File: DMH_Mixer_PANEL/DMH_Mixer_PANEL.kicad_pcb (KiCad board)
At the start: 2 copper layers, 50 x 200 mm, 20 parts, among them J0 Panel_GND_Solder_Wire_Pad

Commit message: Finalization in progress
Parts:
- removed H10: Clip Amt, SynthStuff:MountingHole_TrimPot
- H9: footprint SynthStuff:Jack_6.35mm_Cutout_Output_v6 -> SynthStuff:Toggle_Switch_Cutout
- moved H7 37.8 mm to (58.5, 208.8)
- moved H9 24.8 mm to (91.5, 190.2)
- moved H15 16.5 mm to (75.0, 208.8)
- moved H16 0.75 mm to (83.2, 165.0)
- moved H19 0.75 mm to (58.5, 165.0)
- moved H13 0.50 mm to (83.2, 129.5)
- moved H18 0.50 mm to (58.5, 129.5)
- moved H12 0.25 mm to (83.2, 94.0)
- moved H17 0.25 mm to (58.5, 94.0)

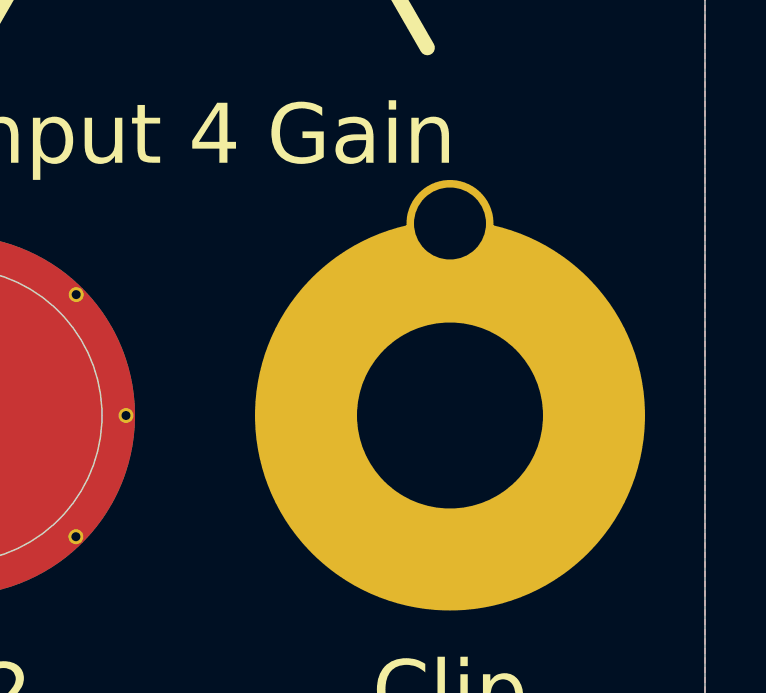
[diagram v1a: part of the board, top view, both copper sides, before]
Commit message: Panel and Connectors PCB ready
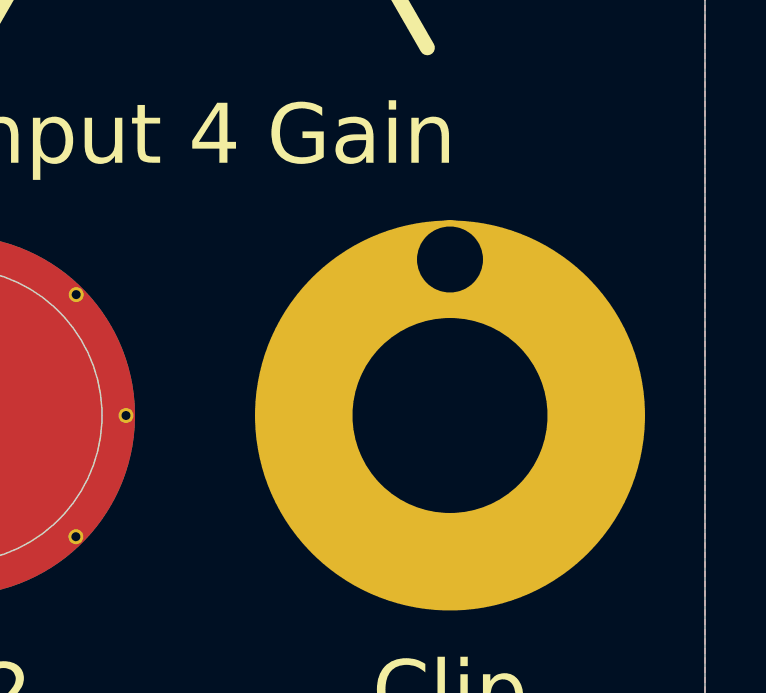
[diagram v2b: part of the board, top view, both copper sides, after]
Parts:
- H9: footprint SynthStuff:Toggle_Switch_Cutout -> SynthStuff:Toggle_Switch_APEM_Cutout
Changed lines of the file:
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@@
 		)
 	)
-	(footprint "SynthStuff:Toggle_Switch_Cutout"
+	(footprint "SynthStuff:Toggle_Switch_APEM_Cutout"
 		(layer "F.Cu")
 		(at 91.5 190.25)
@@
 			)
 		)
-		(property "Footprint" "SynthStuff:Toggle_Switch_Cutout"
+		(property "Footprint" "SynthStuff:Toggle_Switch_APEM_Cutout"
 			(at 0 0 0)
 			(unlocked yes)
@@
 		)
 		(fp_arc
-			(start -6.984267 0)
-			(mid -5.422447 -4.401938)
-			(end -1.435493 -6.835155)
+			(start -7 0)
+			(mid -4.949748 -4.949748)
+			(end 0 -7)
 			(stroke
 				(width 0.05)
@@
 		)
 		(fp_arc
-			(start -1.435493 -6.835156)
-			(mid -0.893663 -7.604727)
-			(end 0 -7.9)
-			(stroke
-				(width 0.05)
-				(type default)
-			)
-			(layer "F.CrtYd")
-		)
-		(fp_arc
-			(start 0 -7.9)
-			(mid 0.893663 -7.604727)
-			(end 1.435493 -6.835156)
-			(stroke
-				(width 0.05)
-				(type default)
-			)
-			(layer "F.CrtYd")
-		)
-		(fp_arc
-			(start 1.435493 -6.835155)
-			(mid 4.401938 5.422446)
-			(end -6.984267 0)
+			(start 0 -7)
+			(mid 4.949747 4.949747)
+			(end -7 0)
 			(stroke
 				(width 0.05)
@@
 		)
 		(pad "1" thru_hole circle
-			(at 0 -6.4)
-			(size 2.9 2.9)
-			(drill 2.4)
+			(at 0 -5.2)
+			(size 2.6 2.6)
+			(drill 2.2)
 			(layers "*.Cu" "*.Mask")
 			(remove_unused_layers no)
@@
 			(at 0 0)
 			(size 13 13)
-			(drill 6.2)
+			(drill 6.5)
 			(layers "*.Cu" "*.Mask")
 			(remove_unused_layers no)

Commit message: Prepared Gerbers for production
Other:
- board text added: "Mk1.0 - December 2024"
- board text removed: "Mk1.0 - Month Year"
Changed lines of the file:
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@@
 			(plot_on_all_layers_selection 0x0000000_00000000)
 			(disableapertmacros no)
-			(usegerberextensions no)
+			(usegerberextensions yes)
 			(usegerberattributes yes)
 			(usegerberadvancedattributes yes)
@@
 			(plotinvisibletext no)
 			(sketchpadsonfab no)
-			(subtractmaskfromsilk no)
+			(subtractmaskfromsilk yes)
 			(outputformat 1)
 			(mirror no)
-			(drillshape 1)
+			(drillshape 0)
 			(scaleselection 1)
-			(outputdirectory "")
+			(outputdirectory "Gerbers/")
 		)
 	)
@@
 		(layer "F.Cu")
 		(at 83.25 129.5)
+		(descr "Based on Alpha RD901F-40-DD0")
 		(property "Reference" "H13"
 			(at 0 -7.9 0)
@@
 		(layer "F.Cu")
 		(at 83.25 58.5)
+		(descr "Based on Alpha RD901F-40-DD0")
 		(property "Reference" "H11"
 			(at 0 -7.9 0)
@@
 		(layer "F.Cu")
 		(at 83.25 94)
+		(descr "Based on Alpha RD901F-40-DD0")
 		(property "Reference" "H12"
 			(at 0 -7.9 0)
@@
 		(layer "F.Cu")
 		(at 83.25 165)
+		(descr "Based on Alpha RD901F-40-DD0")
 		(property "Reference" "H16"
 			(at 0 -7.9 0)
@@
 			(type default)
 		)
-		(layer "Dwgs.User")
+		(layer "F.SilkS")
 	)
 	(gr_line
@@
 			(type default)
 		)
-		(layer "Dwgs.User")
+		(layer "F.SilkS")
 	)
 	(gr_line
@@
 			(type default)
 		)
-		(layer "Dwgs.User")
+		(layer "F.SilkS")
 	)
 	(gr_line
@@
 			(type default)
 		)
-		(layer "Dwgs.User")
+		(layer "F.SilkS")
 	)
 	(gr_line
@@
 		(layer "User.9")
 	)
-	(gr_text "Mk1.0 - Month Year"
+	(gr_text "Mk1.0 - December 2024"
 		(at 75 222.95 0)
 		(layer "B.SilkS")

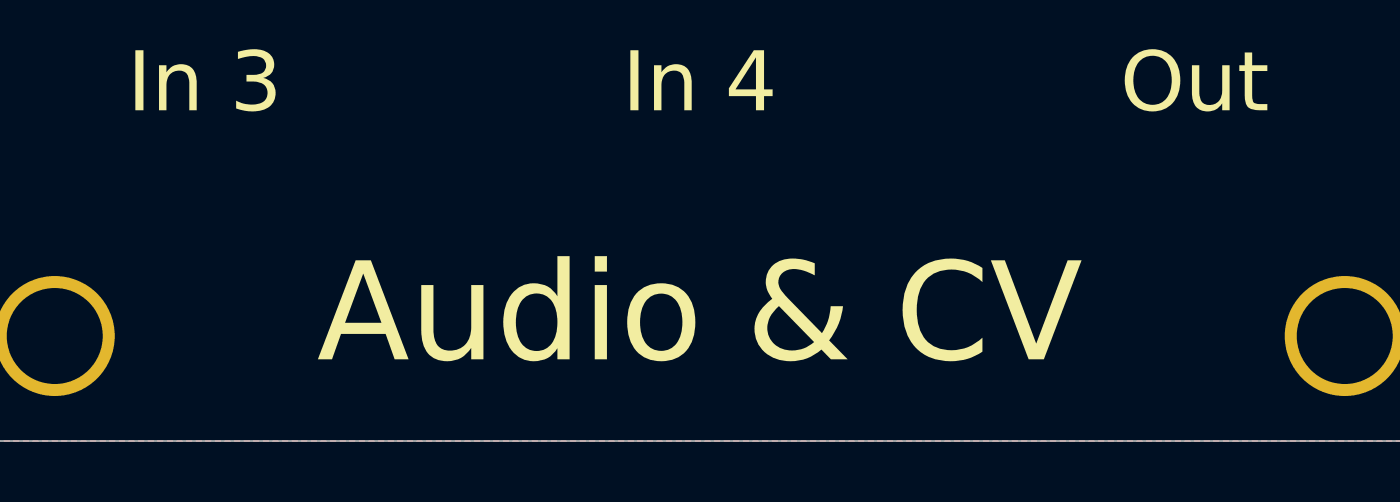
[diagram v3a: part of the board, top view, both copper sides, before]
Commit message: Changed module name to AC & DC in panel
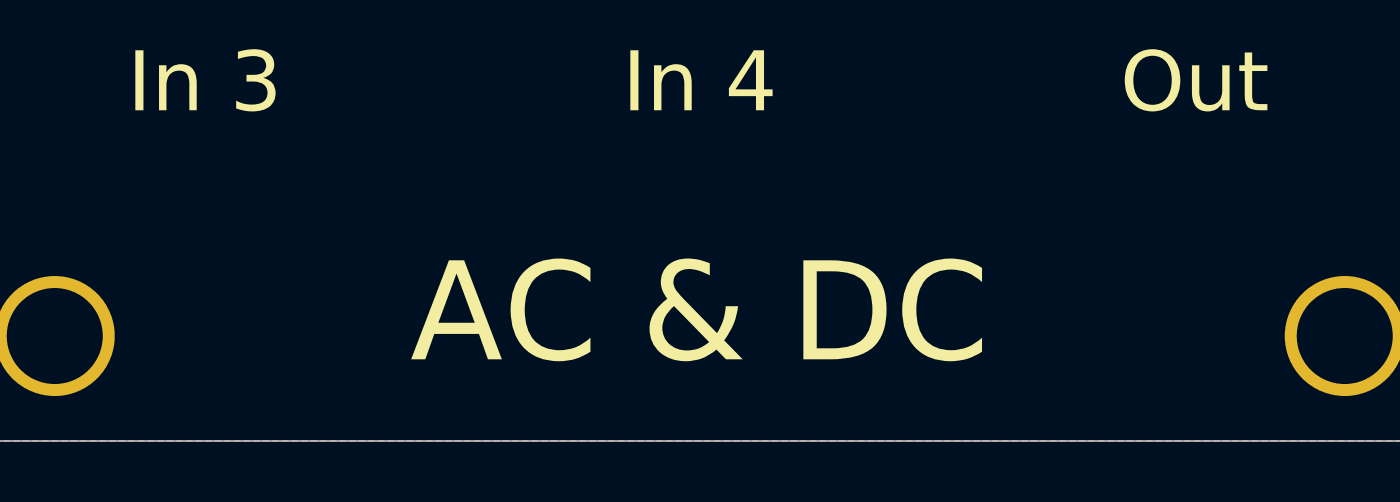
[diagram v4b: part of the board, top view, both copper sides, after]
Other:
- board text added: "AC & DC"
- board text removed: "Audio & CV"
